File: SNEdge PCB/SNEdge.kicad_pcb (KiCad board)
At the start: 2 copper layers, 38.2 x 19.3 mm, 41 parts, among them J1 RGB_OUT, U1 THS7376

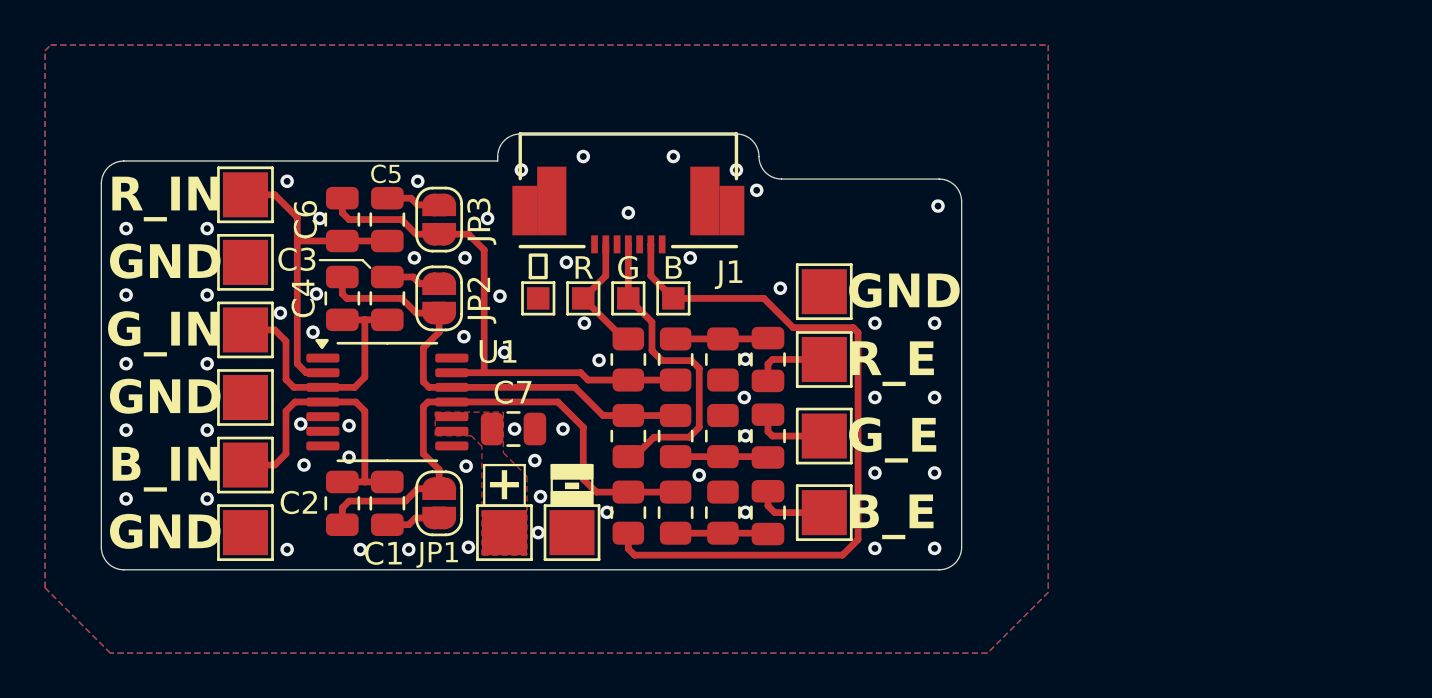
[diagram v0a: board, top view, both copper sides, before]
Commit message: V2 based on RetroLoom's Rev2
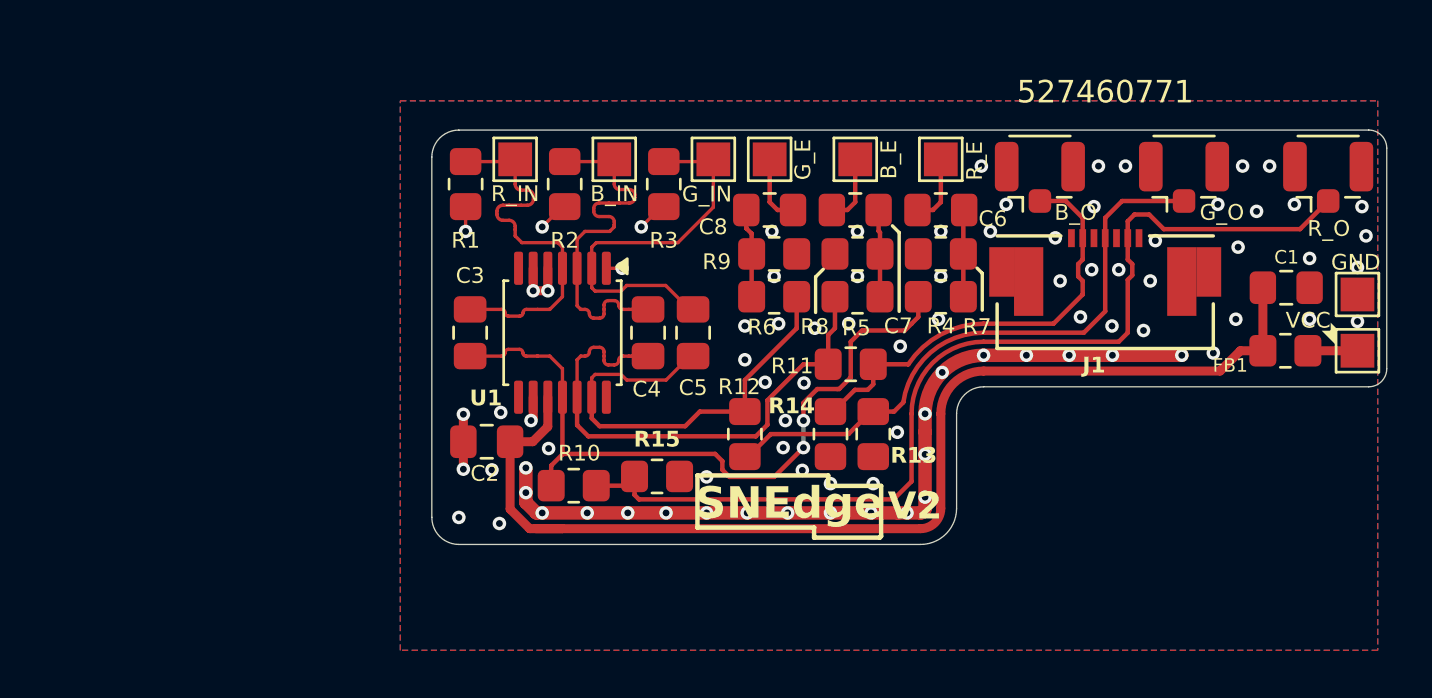
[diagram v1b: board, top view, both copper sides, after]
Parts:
- removed C10, C9: 100nF, Capacitor_SMD:C_0805_2012Metric
- removed the C5 at (129.5, 94.2)
- removed JP1, JP2, JP3: SIDECAR, Jumper:SolderJumper-2_P1.3mm_Open_RoundedPad1.0x1.5mm
- removed REF**: OSHW-Logo_7.5x8mm_SilkScreen, Symbol:OSHW-Logo_7.5x8mm_SilkScreen
- removed TP10: G_OUT, TestPoint:TestPoint_Pad_1.0x1.0mm
- removed TP11: B_OUT, TestPoint:TestPoint_Pad_1.0x1.0mm
- removed TP12: G_ENC, TestPoint:TestPoint_Pad_2.0x2.0mm
- removed TP13: B_ENC, TestPoint:TestPoint_Pad_2.0x2.0mm
- removed TP14: R_ENC, TestPoint:TestPoint_Pad_2.0x2.0mm
- removed TP15: GND, TestPoint:TestPoint_Pad_2.0x2.0mm
- removed TP16: GND, TestPoint:TestPoint_Pad_1.0x1.0mm
- removed TP9: R_OUT, TestPoint:TestPoint_Pad_1.0x1.0mm
- added C7: 1uF, Capacitor_SMD:C_0805_2012Metric_Pad1.18x1.45mm_HandSolder, F.Cu at (150.3, 93.8)
- added FB1: 1k 100MHz, Resistor_SMD:R_0805_2012Metric_Pad1.20x1.40mm_HandSolder, F.Cu at (169.4, 100.0)
- added J10: R_O, Connector_Coaxial:U.FL_Hirose_U.FL-R-SMT-1_Vertical, F.Cu at (171.3, 92.3)
- added J8: G_O, Connector_Coaxial:U.FL_Hirose_U.FL-R-SMT-1_Vertical, F.Cu at (164.9, 92.3)
- added J9: B_O, Connector_Coaxial:U.FL_Hirose_U.FL-R-SMT-1_Vertical, F.Cu at (158.5, 92.3)
- added R10: 249R, Resistor_SMD:R_0805_2012Metric_Pad1.20x1.40mm_HandSolder, F.Cu at (137.8, 106.0)
- added R11: 249R, Resistor_SMD:R_0805_2012Metric_Pad1.20x1.40mm_HandSolder, F.Cu at (150.1, 100.6)
- added R12: 249R, Resistor_SMD:R_0805_2012Metric_Pad1.20x1.40mm_HandSolder, F.Cu at (145.4, 103.7)
- added R13: 107R, Resistor_SMD:R_0805_2012Metric_Pad1.20x1.40mm_HandSolder, F.Cu at (151.1, 103.7)
- added R14: 107R, Resistor_SMD:R_0805_2012Metric_Pad1.20x1.40mm_HandSolder, F.Cu at (149.2, 103.7)
- added R15: 107R, Resistor_SMD:R_0805_2012Metric_Pad1.20x1.40mm_HandSolder, F.Cu at (141.5, 105.6)
- C1: value 3pF -> 22uF; footprint Capacitor_SMD:C_0805_2012Metric -> Capacitor_SMD:C_0805_2012Metric_Pad1.18x1.45mm_HandSolder
- C2, C6: value 24pF -> 1uF; footprint Capacitor_SMD:C_0805_2012Metric -> Capacitor_SMD:C_0805_2012Metric_Pad1.18x1.45mm_HandSolder
- C3: value 3pF -> 15pF; footprint Capacitor_SMD:C_0805_2012Metric -> Capacitor_SMD:C_0805_2012Metric_Pad1.18x1.45mm_HandSolder
- C4: value 24pF -> 15pF; footprint Capacitor_SMD:C_0805_2012Metric -> Capacitor_SMD:C_0805_2012Metric_Pad1.18x1.45mm_HandSolder
- C5: renamed from C7; value 100nF -> 15pF; footprint Capacitor_SMD:C_0805_2012Metric -> Capacitor_SMD:C_0805_2012Metric_Pad1.18x1.45mm_HandSolder
- C8: value 100nF -> 1uF; footprint Capacitor_SMD:C_0805_2012Metric -> Capacitor_SMD:C_0805_2012Metric_Pad1.18x1.45mm_HandSolder
- R1, R3: value 1k -> 7.5k; footprint Resistor_SMD:R_0805_2012Metric -> Resistor_SMD:R_0805_2012Metric_Pad1.20x1.40mm_HandSolder
- R2: value 150R -> 7.5k; footprint Resistor_SMD:R_0805_2012Metric -> Resistor_SMD:R_0805_2012Metric_Pad1.20x1.40mm_HandSolder
- R4: value 150R -> 430R; footprint Resistor_SMD:R_0805_2012Metric -> Resistor_SMD:R_0805_2012Metric_Pad1.20x1.40mm_HandSolder
- R5, R6: value 510R -> 430R; footprint Resistor_SMD:R_0805_2012Metric -> Resistor_SMD:R_0805_2012Metric_Pad1.20x1.40mm_HandSolder
- R7: value 510R -> 75R; footprint Resistor_SMD:R_0805_2012Metric -> Resistor_SMD:R_0805_2012Metric_Pad1.20x1.40mm_HandSolder
- R8: value 1k -> 75R; footprint Resistor_SMD:R_0805_2012Metric -> Resistor_SMD:R_0805_2012Metric_Pad1.20x1.40mm_HandSolder
- R9: value 150R -> 75R; footprint Resistor_SMD:R_0805_2012Metric -> Resistor_SMD:R_0805_2012Metric_Pad1.20x1.40mm_HandSolder
- TP1, TP2, TP5: footprint TestPoint:TestPoint_Pad_2.0x2.0mm -> TestPoint:TestPoint_Pad_1.5x1.5mm
- TP3: value GND -> G_IN; footprint TestPoint:TestPoint_Pad_2.0x2.0mm -> TestPoint:TestPoint_Pad_1.5x1.5mm
- TP4: value GND -> B_IN; footprint TestPoint:TestPoint_Pad_2.0x2.0mm -> TestPoint:TestPoint_Pad_1.5x1.5mm
- TP6: value G_IN -> R_E; footprint TestPoint:TestPoint_Pad_2.0x2.0mm -> TestPoint:TestPoint_Pad_1.5x1.5mm
- TP7: value B_IN -> B_E; footprint TestPoint:TestPoint_Pad_2.0x2.0mm -> TestPoint:TestPoint_Pad_1.5x1.5mm
- TP8: value GND -> G_E; footprint TestPoint:TestPoint_Pad_2.0x2.0mm -> TestPoint:TestPoint_Pad_1.5x1.5mm
- moved C1 41.0 mm to (169.4, 97.2), turned to 180 degrees
- moved TP1 38.7 mm to (172.6, 100.0), turned to 90 degrees
- moved TP2 36.4 mm to (172.6, 97.5), turned to 90 degrees
- moved TP6 31.8 mm to (154.1, 91.5)
- moved TP7 30.3 mm to (150.3, 91.5)
- moved TP8 28.6 mm to (146.5, 91.5)
- moved C6 26.6 mm to (154.1, 93.8), turned to 180 degrees
- moved TP3 23.3 mm to (144.0, 91.5)
- moved J1 21.7 mm to (161.4, 97.4), turned to 0 degrees
- moved R7 18.0 mm to (154.1, 95.7), turned to 180 degrees
- moved TP4 17.0 mm to (139.6, 91.5)
- moved R3 14.6 mm to (141.8, 92.6), turned to 90 degrees
- moved R1 14.6 mm to (133.0, 92.6), turned to 90 degrees
- moved C4 13.7 mm to (141.1, 99.2), turned to 90 degrees
- moved R4 13.6 mm to (154.1, 97.6), turned to 0 degrees
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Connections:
- C1 pad 1: Net-(JP1-A) -> GND
- C1 pad 2: Net-(U1-CH4_IN) -> VCC
- C2 pad 1: Net-(JP1-B) -> GND
- C2 pad 2: Net-(U1-CH4_IN) -> VCC
- C3 pad 1: Net-(JP2-A) -> Net-(U1-CH4_OUT)
- C3 pad 2: Net-(U1-CH3_IN) -> Net-(U1-CH4_IN)
- C4 pad 1: Net-(JP2-B) -> Net-(U1-CH3_OUT)
- C5 pad 1: GND -> Net-(U1-CH2_OUT)
- C5 pad 2: VCC -> Net-(U1-CH2_IN)
- C6 pad 1: Net-(JP3-B) -> Net-(C6-Pad1)
- C6 pad 2: Net-(U1-CH2_IN) -> Net-(C6-Pad2)
- R1 pad 1: Net-(JP2-B) -> GND
- R1 pad 2: Net-(C8-Pad1) -> Net-(U1-CH4_IN)
- R2 pad 1: Net-(C8-Pad1) -> GND
- R2 pad 2: GND -> Net-(U1-CH3_IN)
- R3 pad 1: Net-(JP1-B) -> GND
- R3 pad 2: Net-(C9-Pad1) -> Net-(U1-CH2_IN)
- R4 pad 1: Net-(C9-Pad1) -> Net-(U1-CH4_OUT)
- R4 pad 2: GND -> Net-(C6-Pad1)
- R5 pad 1: Net-(J1-Pin_6) -> Net-(U1-CH3_OUT)
- R5 pad 2: Net-(JP3-B) -> Net-(C7-Pad1)
- R6 pad 1: Net-(J1-Pin_4) -> Net-(U1-CH2_OUT)
- R6 pad 2: Net-(JP2-B) -> Net-(C8-Pad1)
- R7 pad 1: Net-(J1-Pin_2) -> Net-(C6-Pad1)
- R7 pad 2: Net-(JP1-B) -> GND
- R8 pad 1: Net-(JP3-B) -> Net-(C7-Pad1)
- R8 pad 2: Net-(C10-Pad1) -> GND
- R9 pad 1: Net-(C10-Pad1) -> Net-(C8-Pad1)
- TP1 pad 1: VCC -> Net-(FB1-Pad2)
- TP3 pad 1: GND -> Net-(U1-CH2_IN)
- TP4 pad 1: GND -> Net-(U1-CH3_IN)
- TP5 pad 1: Net-(U1-CH2_IN) -> Net-(U1-CH4_IN)
- TP6 pad 1: Net-(U1-CH3_IN) -> Net-(C6-Pad2)
- TP7 pad 1: Net-(U1-CH4_IN) -> Net-(C7-Pad2)
- TP8 pad 1: GND -> Net-(C8-Pad2)
- U1 pad 11: Net-(JP1-B) -> Net-(U1-CH4_OUT)
- U1 pad 12: Net-(JP2-B) -> Net-(U1-CH3_OUT)
- U1 pad 13: Net-(JP3-B) -> Net-(U1-CH2_OUT)
- U1 pad 9: VCC -> GND
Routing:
- net VCC: track 0.00 -> 50.1 mm
- net GND: track 0.10 -> 47.2 mm, vias 62 -> 86
- net Net-(J1-Pin_6): track 5.56 -> 44.8 mm
- net Net-(U1-CH4_OUT): track 0.00 -> 32.4 mm, vias 0 -> 2
- net Net-(JP1-B): track 23.8 -> 0.00 mm
- net Net-(U1-CH3_OUT): track 0.00 -> 23.7 mm
- net Net-(JP3-B): track 23.2 -> 0.00 mm
- net Net-(JP2-B): track 20.6 -> 0.00 mm
- net Net-(U1-CH2_OUT): track 0.00 -> 20.2 mm
- net Net-(J1-Pin_2): track 32.1 -> 15.6 mm
- net Net-(J1-Pin_4): track 13.9 -> 21.8 mm
- net Net-(U1-CH3_IN): track 12.1 -> 17.4 mm
- net Net-(U1-CH4_IN): track 12.9 -> 17.3 mm
- net Net-(C9-Pad1): track 4.12 -> 0.00 mm
- net Net-(C10-Pad1): track 4.12 -> 0.00 mm
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- removed copper zone on F.Cu, net VCC
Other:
- board size 38.2 x 19.3 mm -> 42.4 x 18.4 mm
- board text added: "V2"
- board text removed: "+"
- board text removed: "-"
- board text removed: "B"
- board text removed: "B_E"
- board text removed: "B_IN"
- board text removed: "G"
- board text removed: "GND"
- board text removed: "G_E"
- board text removed: "G_IN"
- board text removed: "R"
- board text removed: "R_E"
- board text removed: "R_IN"
- board text removed: "github.com/ThunderTechnologies/SNEdge"
- board text removed: "⏚"

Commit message: Adjust feedback capacitors to 10pF
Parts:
- C3, C4, C5: value 15pF -> 10pF
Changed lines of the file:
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@@
 			)
 		)
-		(property "Value" "15pF"
+		(property "Value" "10pF"
 			(at 0 1.68 90)
 			(layer "F.Fab")
@@
 			)
 		)
-		(property "Value" "15pF"
+		(property "Value" "10pF"
 			(at 0 1.68 90)
 			(layer "F.Fab")
@@
 			)
 		)
-		(property "Value" "15pF"
+		(property "Value" "10pF"
 			(at 0 1.68 90)
 			(layer "F.Fab")
